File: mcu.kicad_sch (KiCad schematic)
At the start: 19 parts, among them Q4 BC817W, Q5 BC817W, U2 ESP32-WROOM-32

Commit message: Placement concept is finished.
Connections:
- net Disp.SCL: now also U2.12 (IO27); no longer U2.24 (IO2)
- net Disp.SDA: now also U2.11 (IO26); no longer U2.23 (IO15)
- net analog_enable: now also U2.23 (IO15); no longer U2.11 (IO26)
- net onewire_pin: now also U2.24 (IO2); no longer U2.10 (IO25)
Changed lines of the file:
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@@
+	)
+	(no_connect
+		(at 138.43 88.9)
 	)
 	(no_connect
@@
 	)
 	(no_connect
-		(at 138.43 88.9)
+		(at 138.43 99.06)
 	)
 	(no_connect
@@
 	(no_connect
 		(at 107.95 88.9)
-	)
-	(no_connect
-		(at 138.43 104.14)
 	)
 	(no_connect
@@
 		)
 	)
+	(wire
+		(pts
+			(xy 139.7 104.14) (xy 138.43 104.14)
+		)
+		(stroke
+			(width 0)
+			(type default)
+		)
+	)
 	(bus
 		(pts
@@
 	(wire
 		(pts
+			(xy 171.45 78.74) (xy 138.43 78.74)
+		)
+		(stroke
+			(width 0)
+			(type default)
+		)
+	)
+	(wire
+		(pts
 			(xy 138.43 58.42) (xy 227.33 58.42)
 		)
@@
 	(wire
 		(pts
-			(xy 138.43 101.6) (xy 171.45 101.6)
-		)
-		(stroke
-			(width 0)
-			(type default)
-		)
-	)
-	(wire
-		(pts
 			(xy 101.6 36.83) (xy 101.6 38.1)
 		)
@@
 	(wire
 		(pts
-			(xy 139.7 60.96) (xy 138.43 60.96)
-		)
-		(stroke
-			(width 0)
-			(type default)
-		)
-	)
-	(wire
-		(pts
 			(xy 25.4 31.75) (xy 38.1 31.75)
 		)
@@
 	(wire
 		(pts
-			(xy 171.45 101.6) (xy 171.45 132.08)
+			(xy 171.45 78.74) (xy 171.45 132.08)
 		)
 		(stroke
@@
 	(wire
 		(pts
-			(xy 177.8 99.06) (xy 177.8 125.73)
+			(xy 177.8 60.96) (xy 177.8 125.73)
 		)
 		(stroke
@@
 	(wire
 		(pts
-			(xy 139.7 78.74) (xy 138.43 78.74)
-		)
-		(stroke
-			(width 0)
-			(type default)
-		)
-	)
-	(wire
-		(pts
 			(xy 45.72 101.6) (xy 57.15 101.6)
 		)
@@
 	(wire
 		(pts
+			(xy 177.8 60.96) (xy 138.43 60.96)
+		)
+		(stroke
+			(width 0)
+			(type default)
+		)
+	)
+	(wire
+		(pts
 			(xy 71.12 88.9) (xy 77.47 88.9)
 		)
@@
 	(wire
 		(pts
-			(xy 138.43 99.06) (xy 177.8 99.06)
-		)
-		(stroke
-			(width 0)
-			(type default)
-		)
-	)
-	(wire
-		(pts
 			(xy 40.64 101.6) (xy 45.72 101.6)
 		)
@@
 		(pts
 			(xy 45.72 124.46) (xy 45.72 125.73)
+		)
+		(stroke
+			(width 0)
+			(type default)
+		)
+	)
+	(wire
+		(pts
+			(xy 139.7 101.6) (xy 138.43 101.6)
 		)
 		(stroke
@@
 	)
 	(label "Disp.SCL"
-		(at 139.7 60.96 0)
+		(at 139.7 104.14 0)
 		(effects
 			(font
@@
 	)
 	(label "Disp.SDA"
-		(at 139.7 78.74 0)
-		(effects
-			(font
+		(at 139.7 101.6 0)
+		(effects
+			(font

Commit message: Add wiring, change footprint to avoid fatal errors at pads.
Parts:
- renumbered C17 to C14, C11 to C15, C9 to C16, C10 to C17, D5 to D3, Q4 to Q6, Q5 to Q7, R35 to R21, R40 to R22, R19 to R23, R20 to R24, R33 to R25, R34 to R26, R14 to R27, R18 to R28, R15 to R29, R17 to R30, R16 to R31, U2 to U4
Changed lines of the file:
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@@
 		(dnp no)
 		(fields_autoplaced yes)
-		(property "Reference" "#PWR013"
+		(property "Reference" "#PWR040"
 			(at 38.1 44.45 0)
 			(hide yes)
@@
 			(project "MoistureESP"
 				(path "/f2b9f638-139e-46ec-aa60-77c4af989196/0ddaa739-ba4f-4157-bc77-184906368825"
-					(reference "#PWR013")
+					(reference "#PWR040")
 					(unit 1)
 				)
@@
 		(dnp no)
 		(fields_autoplaced yes)
-		(property "Reference" "R20"
+		(property "Reference" "R24"
 			(at 46.99 76.2 90)
 			(show_name no)
@@
 			(project "MoistureESP"
 				(path "/f2b9f638-139e-46ec-aa60-77c4af989196/0ddaa739-ba4f-4157-bc77-184906368825"
-					(reference "R20")
+					(reference "R24")
 					(unit 1)
 				)
@@
 		(in_pos_files yes)
 		(dnp no)
-		(property "Reference" "Q5"
+		(property "Reference" "Q7"
 			(at 73.66 83.8201 0)
 			(show_name no)
@@
 			(project "MoistureESP"
 				(path "/f2b9f638-139e-46ec-aa60-77c4af989196/0ddaa739-ba4f-4157-bc77-184906368825"
-					(reference "Q5")
+					(reference "Q7")
 					(unit 1)
 				)
@@
 		(dnp no)
 		(fields_autoplaced yes)
-		(property "Reference" "R19"
+		(property "Reference" "R23"
 			(at 46.99 57.15 90)
 			(show_name no)
@@
 			(project "MoistureESP"
 				(path "/f2b9f638-139e-46ec-aa60-77c4af989196/0ddaa739-ba4f-4157-bc77-184906368825"
-					(reference "R19")
+					(reference "R23")
 					(unit 1)
 				)
@@
 		(in_pos_files yes)
 		(dnp no)
-		(property "Reference" "R15"
+		(property "Reference" "R29"
 			(at 197.866 85.09 0)
 			(show_name no)
@@
 			(project "MoistureESP"
 				(path "/f2b9f638-139e-46ec-aa60-77c4af989196/0ddaa739-ba4f-4157-bc77-184906368825"
-					(reference "R15")
+					(reference "R29")
 					(unit 1)
 				)
@@
 		(dnp no)
 		(fields_autoplaced yes)
-		(property "Reference" "#PWR019"
+		(property "Reference" "#PWR048"
 			(at 185.42 76.2 0)
 			(hide yes)
@@
 			(project "MoistureESP"
 				(path "/f2b9f638-139e-46ec-aa60-77c4af989196/0ddaa739-ba4f-4157-bc77-184906368825"
-					(reference "#PWR019")
+					(reference "#PWR048")
 					(unit 1)
 				)
@@
 		(dnp no)
 		(fields_autoplaced yes)
-		(property "Reference" "C10"
+		(property "Reference" "C17"
 			(at 118.11 31.7499 0)
 			(show_name no)
@@
 			(project "MoistureESP"
 				(path "/f2b9f638-139e-46ec-aa60-77c4af989196/0ddaa739-ba4f-4157-bc77-184906368825"
-					(reference "C10")
+					(reference "C17")
 					(unit 1)
 				)
@@
 		(dnp no)
 		(fields_autoplaced yes)
-		(property "Reference" "U2"
+		(property "Reference" "U4"
 			(at 125.3333 48.26 0)
 			(show_name no)
@@
 			(project "MoistureESP"
 				(path "/f2b9f638-139e-46ec-aa60-77c4af989196/0ddaa739-ba4f-4157-bc77-184906368825"
-					(reference "U2")
+					(reference "U4")
 					(unit 1)
 				)
@@
 		(dnp no)
 		(fields_autoplaced yes)
-		(property "Reference" "#PWR046"
+		(property "Reference" "#PWR041"
 			(at 45.72 132.08 0)
 			(hide yes)
@@
 			(project "MoistureESP"
 				(path "/f2b9f638-139e-46ec-aa60-77c4af989196/0ddaa739-ba4f-4157-bc77-184906368825"
-					(reference "#PWR046")
+					(reference "#PWR041")
 					(unit 1)
 				)
@@
 		(dnp no)
 		(fields_autoplaced yes)
-		(property "Reference" "#PWR011"
+		(property "Reference" "#PWR046"
 			(at 101.6 45.72 0)
 			(hide yes)
@@
 			(project "MoistureESP"
 				(path "/f2b9f638-139e-46ec-aa60-77c4af989196/0ddaa739-ba4f-4157-bc77-184906368825"
-					(reference "#PWR011")
+					(reference "#PWR046")
 					(unit 1)
 				)
@@
 		(dnp no)
 		(fields_autoplaced yes)
-		(property "Reference" "R34"
+		(property "Reference" "R26"
 			(at 81.28 153.6699 0)
 			(show_name no)
@@
 			(project "MoistureESP"
 				(path "/f2b9f638-139e-46ec-aa60-77c4af989196/0ddaa739-ba4f-4157-bc77-184906368825"
-					(reference "R34")
+					(reference "R26")
 					(unit 1)
 				)
@@
 		(dnp no)
 		(fields_autoplaced yes)
-		(property "Reference" "#PWR015"
+		(property "Reference" "#PWR045"
 			(at 88.9 73.66 0)
 			(hide yes)
@@
 			(project "MoistureESP"
 				(path "/f2b9f638-139e-46ec-aa60-77c4af989196/0ddaa739-ba4f-4157-bc77-184906368825"
-					(reference "#PWR015")
+					(reference "#PWR045")
 					(unit 1)
 				)
@@
 		(dnp no)
 		(fields_autoplaced yes)
-		(property "Reference" "R14"
+		(property "Reference" "R27"
 			(at 91.44 38.0999 0)
 			(show_name no)
@@
 			(project "MoistureESP"
 				(path "/f2b9f638-139e-46ec-aa60-77c4af989196/0ddaa739-ba4f-4157-bc77-184906368825"
-					(reference "R14")
+					(reference "R27")
 					(unit 1)
 				)
@@
 		(dnp no)
 		(fields_autoplaced yes)
-		(property "Reference" "#PWR017"
+		(property "Reference" "#PWR042"
 			(at 63.5 25.4 0)
 			(hide yes)
@@
 			(project "MoistureESP"
 				(path "/f2b9f638-139e-46ec-aa60-77c4af989196/0ddaa739-ba4f-4157-bc77-184906368825"
-					(reference "#PWR017")
+					(reference "#PWR042")
 					(unit 1)
 				)
@@
 		(dnp no)
 		(fields_autoplaced yes)
-		(property "Reference" "#PWR020"
+		(property "Reference" "#PWR043"
 			(at 78.74 151.13 0)
 			(hide yes)
@@
 			(project "MoistureESP"
 				(path "/f2b9f638-139e-46ec-aa60-77c4af989196/0ddaa739-ba4f-4157-bc77-184906368825"
-					(reference "#PWR020")
+					(reference "#PWR043")
 					(unit 1)
 				)
@@
 		(dnp no)
 		(fields_autoplaced yes)
-		(property "Reference" "Q4"
+		(property "Reference" "Q6"
 			(at 73.66 62.2299 0)
 			(show_name no)
@@
 			(project "MoistureESP"
 				(path "/f2b9f638-139e-46ec-aa60-77c4af989196/0ddaa739-ba4f-4157-bc77-184906368825"
-					(reference "Q4")
+					(reference "Q6")
 					(unit 1)
 				)
@@
 		(in_pos_files yes)
 		(dnp no)
-		(property "Reference" "R16"
+		(property "Reference" "R31"
 			(at 210.566 85.09 0)
 			(show_name no)
@@
 			(project "MoistureESP"
 				(path "/f2b9f638-139e-46ec-aa60-77c4af989196/0ddaa739-ba4f-4157-bc77-184906368825"
-					(reference "R16")
+					(reference "R31")
 					(unit 1)
 				)
@@
 		(dnp yes)
 		(fields_autoplaced yes)
-		(property "Reference" "R40"
+		(property "Reference" "R22"
 			(at 48.26 111.7599 0)
 			(show_name no)
@@
 			(project "MoistureESP"
 				(path "/f2b9f638-139e-46ec-aa60-77c4af989196/0ddaa739-ba4f-4157-bc77-184906368825"
-					(reference "R40")
+					(reference "R22")
 					(unit 1)
 				)
@@
 		(dnp no)
 		(fields_autoplaced yes)
-		(property "Reference" "C17"
+		(property "Reference" "C14"
 			(at 82.55 168.9099 0)
 			(show_name no)
@@
 			(project "MoistureESP"
 				(path "/f2b9f638-139e-46ec-aa60-77c4af989196/0ddaa739-ba4f-4157-bc77-184906368825"
-					(reference "C17")
+					(reference "C14")
 					(unit 1)
 				)
@@
 		(dnp yes)
 		(fields_autoplaced yes)
-		(property "Reference" "R35"
+		(property "Reference" "R21"
 			(at 36.83 95.25 90)
 			(show_name no)
@@
 			(project "MoistureESP"
 				(path "/f2b9f638-139e-46ec-aa60-77c4af989196/0ddaa739-ba4f-4157-bc77-184906368825"
-					(reference "R35")
+					(reference "R21")
 					(unit 1)
 				)
@@
 		(dnp no)
 		(fields_autoplaced yes)
-		(property "Reference" "R33"
+		(property "Reference" "R25"
 			(at 59.69 158.75 90)
 			(show_name no)
@@
 			(project "MoistureESP"
 				(path "/f2b9f638-139e-46ec-aa60-77c4af989196/0ddaa739-ba4f-4157-bc77-184906368825"
-					(reference "R33")
+					(reference "R25")
 					(unit 1)
 				)
@@
 		(dnp no)
 		(fields_autoplaced yes)
-		(property "Reference" "#PWR010"
+		(property "Reference" "#PWR047"
 			(at 123.19 133.35 0)
 			(hide yes)
@@
 			(project "MoistureESP"
 				(path "/f2b9f638-139e-46ec-aa60-77c4af989196/0ddaa739-ba4f-4157-bc77-184906368825"
-					(reference "#PWR010")
+					(reference "#PWR047")
 					(unit 1)
 				)
@@
 		(in_pos_files yes)
 		(dnp no)
-		(property "Reference" "R18"
+		(property "Reference" "R28"
 			(at 191.516 85.09 0)
 			(show_name no)
@@
 			(project "MoistureESP"
 				(path "/f2b9f638-139e-46ec-aa60-77c4af989196/0ddaa739-ba4f-4157-bc77-184906368825"
-					(reference "R18")
+					(reference "R28")
 					(unit 1)
 				)
@@
 		(dnp no)
 		(fields_autoplaced yes)
-		(property "Reference" "C11"
+		(property "Reference" "C15"
 			(at 92.71 60.9599 0)
 			(show_name no)
@@
 			(project "MoistureESP"
 				(path "/f2b9f638-139e-46ec-aa60-77c4af989196/0ddaa739-ba4f-4157-bc77-184906368825"
-					(reference "C11")
+					(reference "C15")
 					(unit 1)
 				)
@@
 		(dnp no)
 		(fields_autoplaced yes)
-		(property "Reference" "C9"
+		(property "Reference" "C16"
 			(at 105.41 31.7499 0)
 			(show_name no)
@@
 			(project "MoistureESP"
 				(path "/f2b9f638-139e-46ec-aa60-77c4af989196/0ddaa739-ba4f-4157-bc77-184906368825"
-					(reference "C9")
+					(reference "C16")
 					(unit 1)
 				)
@@
 		(in_pos_files yes)
 		(dnp no)
-		(property "Reference" "R17"
+		(property "Reference" "R30"
 			(at 204.216 85.09 0)
 			(show_name no)
@@
 			(project "MoistureESP"
 				(path "/f2b9f638-139e-46ec-aa60-77c4af989196/0ddaa739-ba4f-4157-bc77-184906368825"
-					(reference "R17")
+					(reference "R30")
 					(unit 1)
 				)
@@
 		(dnp yes)
 		(fields_autoplaced yes)
-		(property "Reference" "D5"
+		(property "Reference" "D3"
 			(at 59.69 111.7599 90)
 			(show_name no)
@@
 			(project "MoistureESP"
 				(path "/f2b9f638-139e-46ec-aa60-77c4af989196/0ddaa739-ba4f-4157-bc77-184906368825"
-					(reference "D5")
-					(unit 1)
-				)
+					(reference "D3")
+					(unit 1)
+				)

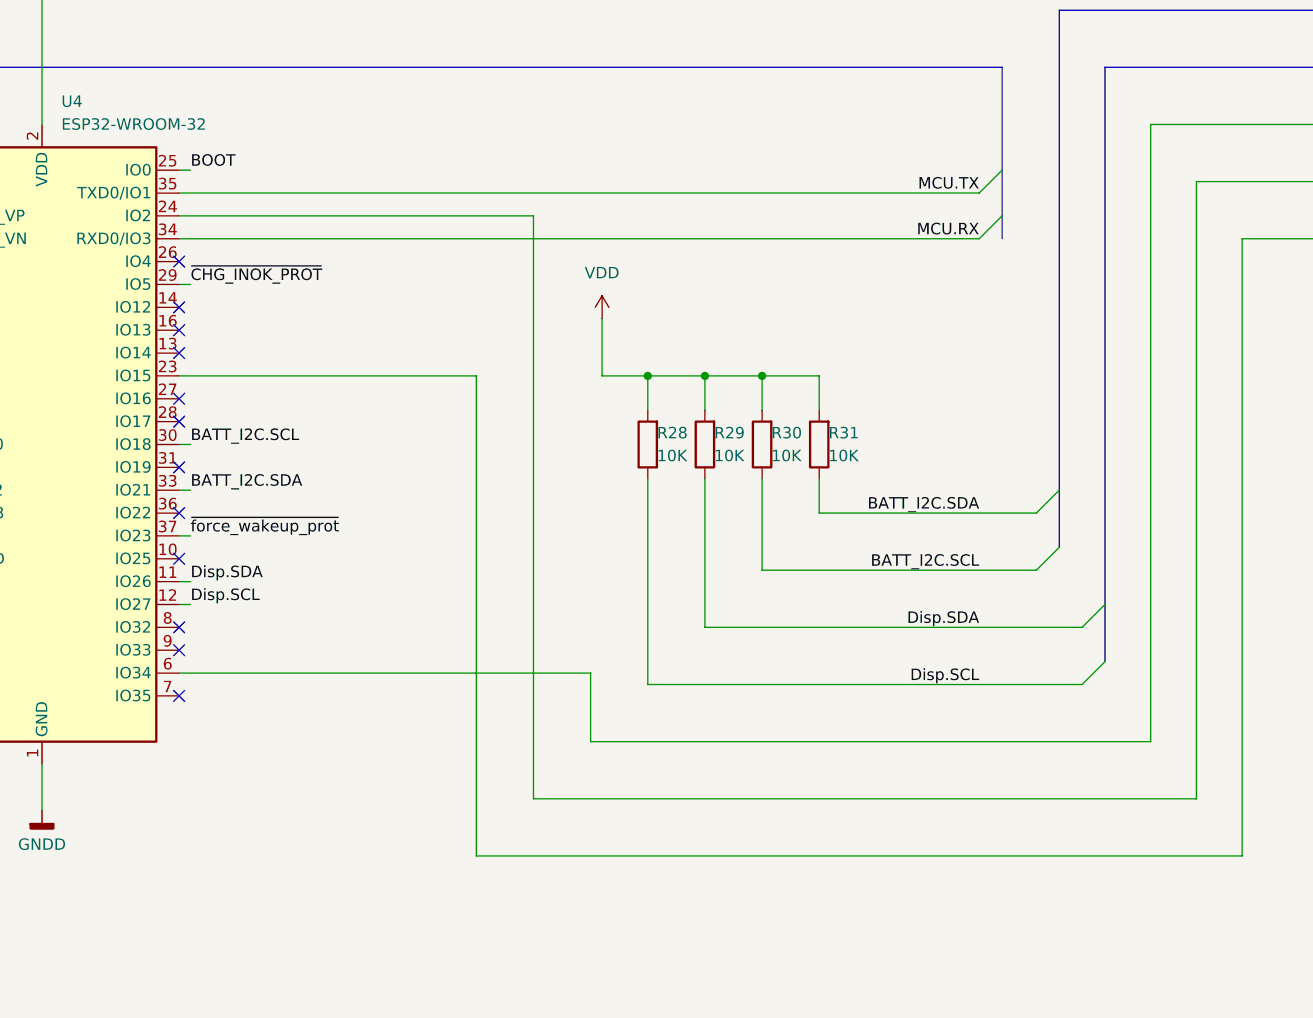
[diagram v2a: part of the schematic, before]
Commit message: Fix ESP32 GPIO wiring, many bootstrap pins were used.
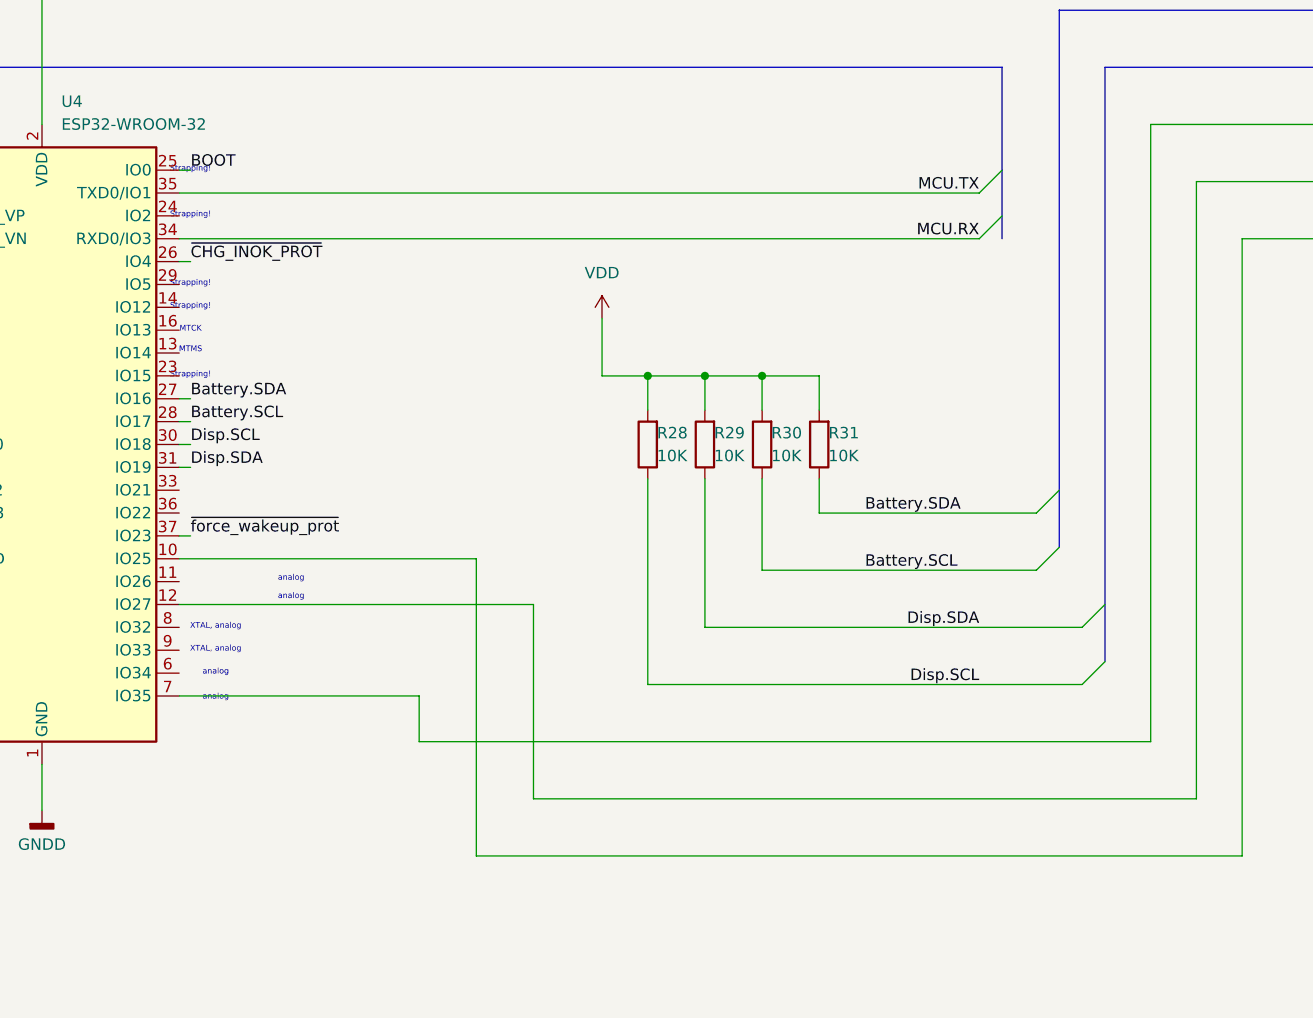
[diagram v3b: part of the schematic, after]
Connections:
- net Disp.SCL: now also U4.30 (IO18); no longer U4.12 (IO27)
- net Disp.SDA: now also U4.31 (IO19); no longer U4.11 (IO26)
- net analog_enable: now also U4.10 (IO25); no longer U4.23 (IO15)
- net analog_pin: now also U4.7 (IO35); no longer U4.6 (IO34)
- net onewire_pin: now also U4.12 (IO27); no longer U4.24 (IO2)
- net ~{CHG_INOK_PROT}: now also U4.26 (IO4); no longer U4.29 (IO5)
- net Battery.SDA: now reaches U4.27 (IO16)
- net Battery.SDA: now also R31.1
- net Battery.SCL: now reaches U4.28 (IO17)
- net Battery.SCL: now also R30.1
- removed net BATT_I2C.SCL: R30.1, U4.30 (IO18)
- net BATT_I2C.SDA: no longer names the net of U4.33 (IO21)
- net BATT_I2C.SDA: no longer R31.1
- no-connect marks 20 -> 8
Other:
- note added: "MTCK"
- note added: "MTMS"
- note added: "Strapping!"
- note added: "XTAL, analog"
- note added: "analog"
